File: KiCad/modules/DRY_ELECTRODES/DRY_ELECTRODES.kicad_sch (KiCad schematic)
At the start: 8 parts, among them J1 Conn_01x01_Pin, J2 Conn_01x01_Pin, J3 Conn_01x01_Pin, J4 Conn_01x01_Pin, J5 Conn_01x01_Pin, J6 Conn_01x01_Pin, J7 Conn_01x01_Pin, J8 Conn_01x01_Pin

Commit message: lot of updates on ads93,flex,commod,pad
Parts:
- added I1, I2, I3, I4: smd_insert, 00_Custom:insert_1.2mm, symbol 00_custom:smd_insert
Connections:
- net in2: now reaches J2.1 (Pin_1)
- net in3: now reaches J3.1 (Pin_1)
- net in4: now reaches J4.1 (Pin_1)
- net in1: now reaches J1.1 (Pin_1)
- net in5: now reaches J5.1 (Pin_1)
- net in8: now reaches J8.1 (Pin_1)
- net in7: now reaches J7.1 (Pin_1)
- net in6: now reaches J6.1 (Pin_1)
- new net GND: I1.1 (conn), I2.1 (conn), I3.1 (conn), I4.1 (conn)
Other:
- moved on the sheet: J1, J2, J3, J4, J5, J6, J7, J8

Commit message: INA331 IMUICM
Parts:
- added J10, J11, J12, J13, J14, J15, J16, J9: Conn_01x01_Pin, 00_custom-footprints:SolderWirePad_1x01_SMD_1x2mm, symbol Connector:Conn_01x01_Pin
- I1, I2, I3, I4: footprint 00_Custom:insert_1.2mm -> 00_custom-footprints:insert_1.2mm
- J1, J2, J3, J4, J5, J6, J7, J8: footprint Connector_Wire:SolderWirePad_1x01_SMD_1x2mm -> 00_custom-footprints:SolderWirePad_1x01_SMD_1x2mm
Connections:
- net in1 renamed in1-
- net in2 renamed in2-
- net in3 renamed in3-
- net in4 renamed in4-
- net in5 renamed in5-
- net in6 renamed in6-
- net in7 renamed in7-
- net in8 renamed in8-
- new net in1+: J9.1 (Pin_1)
- new net in2+: J10.1 (Pin_1)
- new net in3+: J11.1 (Pin_1)
- new net in4+: J12.1 (Pin_1)
- new net in5+: J13.1 (Pin_1)
- new net in6+: J14.1 (Pin_1)
- new net in7+: J15.1 (Pin_1)
- new net in8+: J16.1 (Pin_1)

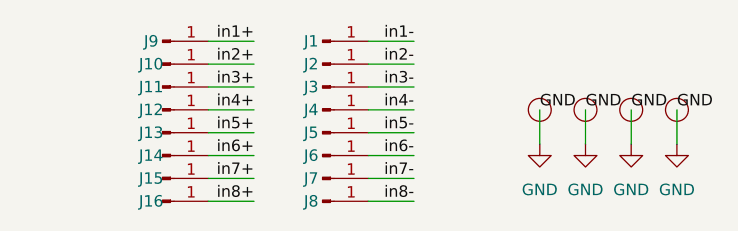
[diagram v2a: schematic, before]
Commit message: jack, dry electrode
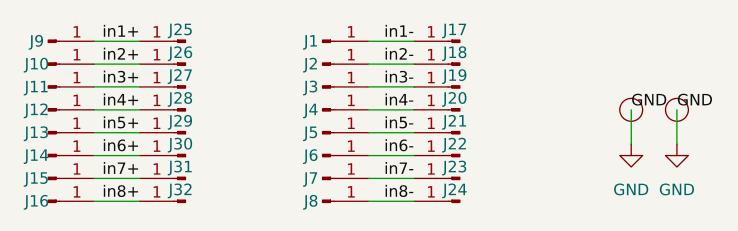
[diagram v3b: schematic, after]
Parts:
- removed I1, I2: smd_insert, 00_custom-footprints:insert_1.2mm, symbol 00_custom:smd_insert
- added J17, J18, J19, J20, J21, J22, J23, J24, J25, J26, J27, J28, J29, J30, J31, J32: Conn_01x01_Pin, 00_custom-footprints:Pin_D1.2mm_pogo, symbol Connector:Conn_01x01_Pin
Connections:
- net in1+: now also J25.1 (Pin_1)
- net in1-: now also J17.1 (Pin_1)
- net in2+: now also J26.1 (Pin_1)
- net in2-: now also J18.1 (Pin_1)
- net in3+: now also J27.1 (Pin_1)
- net in3-: now also J19.1 (Pin_1)
- net in4+: now also J28.1 (Pin_1)
- net in4-: now also J20.1 (Pin_1)
- net in5+: now also J29.1 (Pin_1)
- net in5-: now also J21.1 (Pin_1)
- net in6+: now also J30.1 (Pin_1)
- net in6-: now also J22.1 (Pin_1)
- net in7+: now also J31.1 (Pin_1)
- net in7-: now also J23.1 (Pin_1)
- net in8+: now also J32.1 (Pin_1)
- net in8-: now also J24.1 (Pin_1)
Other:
- moved on the sheet: J10, J11, J12, J13, J14, J15, J16, J9

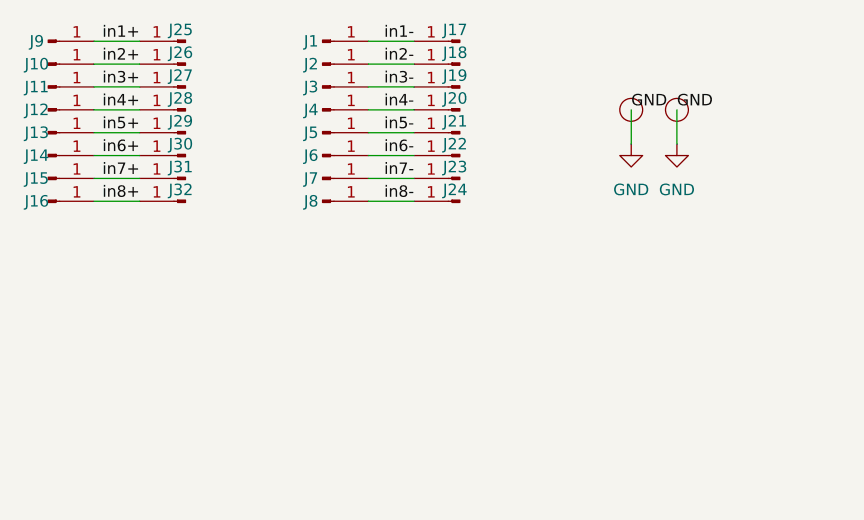
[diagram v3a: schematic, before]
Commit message: refactor and fixing most of the modules
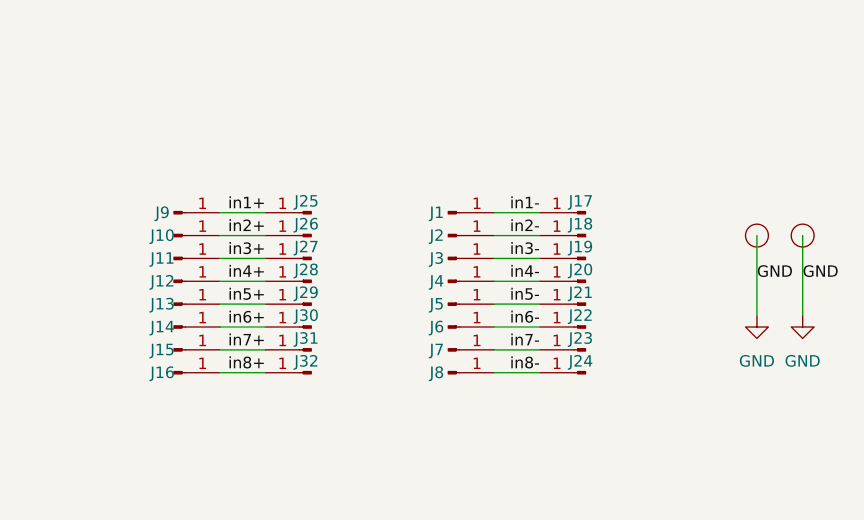
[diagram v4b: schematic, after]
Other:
- company: (none) -> Aightech
- title: (none) -> Dry Electrodes
- moved on the sheet: J1, J10, J11, J12, J13, J14, J15, J16, J17, J18, J19, J2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
